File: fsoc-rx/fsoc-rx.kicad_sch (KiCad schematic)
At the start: 0 parts

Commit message: RX ROOT: power USB
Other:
- added sheet RX_POWER_USB (rx_power_usb.kicad_sch)
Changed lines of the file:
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@@
 	(generator_version "10.0")
 	(paper "A4")
+	(sheet
+		(at 44.45 35.56)
+		(size 54.61 88.9)
+		(exclude_from_sim no)
+		(in_bom yes)
+		(on_board yes)
+		(dnp no)
+		(fields_autoplaced yes)
+		(stroke
+			(width 0.1524)
+			(type solid)
+		)
+		(fill
+			(color 0 0 0 0)
+		)
+		(property "Sheetname" "RX_POWER_USB"
+			(at 44.45 34.8484 0)
+			(show_name no)
+			(do_not_autoplace no)
+			(effects
+				(font
+					(size 1.27 1.27)
+				)
+				(justify left bottom)
+			)
+		)
+		(property "Sheetfile" "rx_power_usb.kicad_sch"
+			(at 44.45 125.0446 0)
+			(show_name no)
+			(do_not_autoplace no)
+			(effects
+				(font
+					(size 1.27 1.27)
+				)
+				(justify left top)
+			)
+		)
+		(instances
+			(project "fsoc-rx"
+				(path "/84f983f4-ce6f-4382-bffe-129758307136"
+					(page "2")
+				)
+			)
+		)
+	)
 	(sheet_instances
 		(path "/"

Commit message: RX ROOT: MCU clock
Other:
- added sheet RX_MCU_CLOCK (rx_mcu_clock.kicad_sch)
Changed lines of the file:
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@@
+		)
+	)
+	(sheet
+		(at 139.7 46.99)
+		(size 63.5 74.93)
+		(exclude_from_sim no)
+		(in_bom yes)
+		(on_board yes)
+		(dnp no)
+		(fields_autoplaced yes)
+		(stroke
+			(width 0.1524)
+			(type solid)
+		)
+		(fill
+			(color 0 0 0 0)
+		)
+		(property "Sheetname" "RX_MCU_CLOCK"
+			(at 139.7 46.2784 0)
+			(show_name no)
+			(do_not_autoplace no)
+			(effects
+				(font
+					(size 1.27 1.27)
+				)
+				(justify left bottom)
+			)
+		)
+		(property "Sheetfile" "rx_mcu_clock.kicad_sch"
+			(at 139.7 122.5046 0)
+			(show_name no)
+			(do_not_autoplace no)
+			(effects
+				(font
+					(size 1.27 1.27)
+				)
+				(justify left top)
+			)
+		)
+		(instances
+			(project "fsoc-rx"
+				(path "/84f983f4-ce6f-4382-bffe-129758307136"
+					(page "3")
+				)
+			)
 		)
 	)

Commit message: RX ROOT: HOST IO
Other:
- added sheet RX_HOST_IO (rx_host_io.kicad_sch)
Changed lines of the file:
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@@
 	(paper "A4")
 	(sheet
+		(at 60.96 90.17)
+		(size 49.53 21.59)
+		(exclude_from_sim no)
+		(in_bom yes)
+		(on_board yes)
+		(dnp no)
+		(fields_autoplaced yes)
+		(stroke
+			(width 0.1524)
+			(type solid)
+		)
+		(fill
+			(color 0 0 0 0)
+		)
+		(property "Sheetname" "RX_HOST_IO"
+			(at 60.96 89.4584 0)
+			(show_name no)
+			(do_not_autoplace no)
+			(effects
+				(font
+					(size 1.27 1.27)
+				)
+				(justify left bottom)
+			)
+		)
+		(property "Sheetfile" "rx_host_io.kicad_sch"
+			(at 60.96 112.3446 0)
+			(show_name no)
+			(do_not_autoplace no)
+			(effects
+				(font
+					(size 1.27 1.27)
+				)
+				(justify left top)
+			)
+		)
+		(instances
+			(project "fsoc-rx"
+				(path "/84f983f4-ce6f-4382-bffe-129758307136"
+					(page "4")
+				)
+			)
+		)
+	)
+	(sheet
 		(at 44.45 35.56)
-		(size 54.61 88.9)
+		(size 57.15 27.94)
 		(exclude_from_sim no)
 		(in_bom yes)
@@
 		)
 		(property "Sheetfile" "rx_power_usb.kicad_sch"
-			(at 44.45 125.0446 0)
+			(at 44.45 64.0846 0)
 			(show_name no)
 			(do_not_autoplace no)
@@
 	)
 	(sheet
-		(at 139.7 46.99)
-		(size 63.5 74.93)
+		(at 124.46 36.83)
+		(size 57.15 30.48)
 		(exclude_from_sim no)
 		(in_bom yes)
@@
 		)
 		(property "Sheetname" "RX_MCU_CLOCK"
-			(at 139.7 46.2784 0)
+			(at 124.46 36.1184 0)
 			(show_name no)
 			(do_not_autoplace no)
@@
 		)
 		(property "Sheetfile" "rx_mcu_clock.kicad_sch"
-			(at 139.7 122.5046 0)
+			(at 124.46 67.8946 0)
 			(show_name no)
 			(do_not_autoplace no)

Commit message: RX ROOT: monitor
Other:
- added sheet RX_MONITOR (rx_monitor.kicad_sch)
- added sheet RX_OPTICAL_AFE (rx_optical_afe.kicad_sch)
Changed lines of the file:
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@@
 	(paper "A4")
 	(sheet
-		(at 60.96 90.17)
+		(at 44.45 83.82)
 		(size 49.53 21.59)
 		(exclude_from_sim no)
@@
 		)
 		(property "Sheetname" "RX_HOST_IO"
-			(at 60.96 89.4584 0)
+			(at 44.45 83.1084 0)
 			(show_name no)
 			(do_not_autoplace no)
@@
 		)
 		(property "Sheetfile" "rx_host_io.kicad_sch"
-			(at 60.96 112.3446 0)
+			(at 44.45 105.9946 0)
 			(show_name no)
 			(do_not_autoplace no)
@@
 				(path "/84f983f4-ce6f-4382-bffe-129758307136"
 					(page "4")
+				)
+			)
+		)
+	)
+	(sheet
+		(at 118.11 85.09)
+		(size 59.69 20.32)
+		(exclude_from_sim no)
+		(in_bom yes)
+		(on_board yes)
+		(dnp no)
+		(fields_autoplaced yes)
+		(stroke
+			(width 0.1524)
+			(type solid)
+		)
+		(fill
+			(color 0 0 0 0)
+		)
+		(property "Sheetname" "RX_OPTICAL_AFE"
+			(at 118.11 84.3784 0)
+			(show_name no)
+			(do_not_autoplace no)
+			(effects
+				(font
+					(size 1.27 1.27)
+				)
+				(justify left bottom)
+			)
+		)
+		(property "Sheetfile" "rx_optical_afe.kicad_sch"
+			(at 118.11 105.9946 0)
+			(show_name no)
+			(do_not_autoplace no)
+			(effects
+				(font
+					(size 1.27 1.27)
+				)
+				(justify left top)
+			)
+		)
+		(instances
+			(project "fsoc-rx"
+				(path "/84f983f4-ce6f-4382-bffe-129758307136"
+					(page "5")
 				)
 			)
@@
 				)
 			)
+		)
+	)
+	(sheet
+		(at 45.72 125.73)
+		(size 50.8 20.32)
+		(exclude_from_sim no)
+		(in_bom yes)
+		(on_board yes)
+		(dnp no)
+		(fields_autoplaced yes)
+		(stroke
+			(width 0.1524)
+			(type solid)
+		)
+		(fill
+			(color 0 0 0 0)
+		)
+		(property "Sheetname" "RX_MONITOR"
+			(at 45.72 125.0184 0)
+			(show_name no)
+			(do_not_autoplace no)
+			(effects
+				(font
+					(size 1.27 1.27)
+				)
+				(justify left bottom)
+			)
+		)
+		(property "Sheetfile" "rx_monitor.kicad_sch"
+			(at 45.72 146.6346 0)
+			(show_name no)
+			(do_not_autoplace no)
+			(effects
+				(font
+					(size 1.27 1.27)
+				)
+				(justify left top)
+			)
+		)
+		(instances
+			(project "fsoc-rx"
+				(path "/84f983f4-ce6f-4382-bffe-129758307136"
+					(page "6")
+				)
+			)

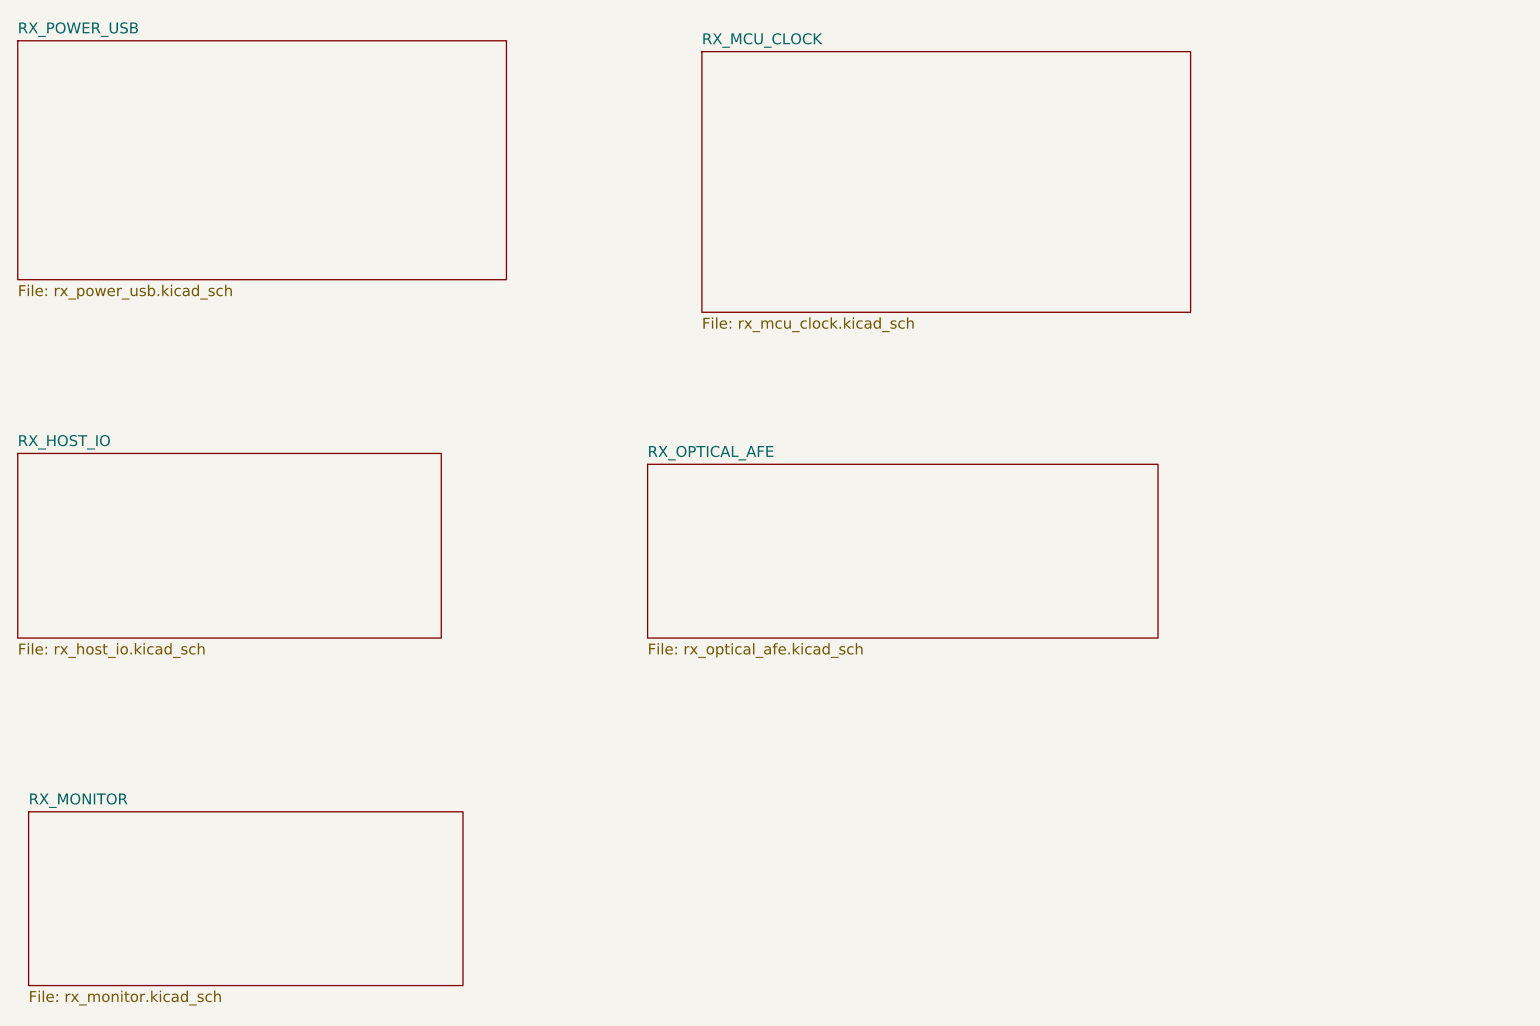
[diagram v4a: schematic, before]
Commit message: RX ROOT: optical AFE
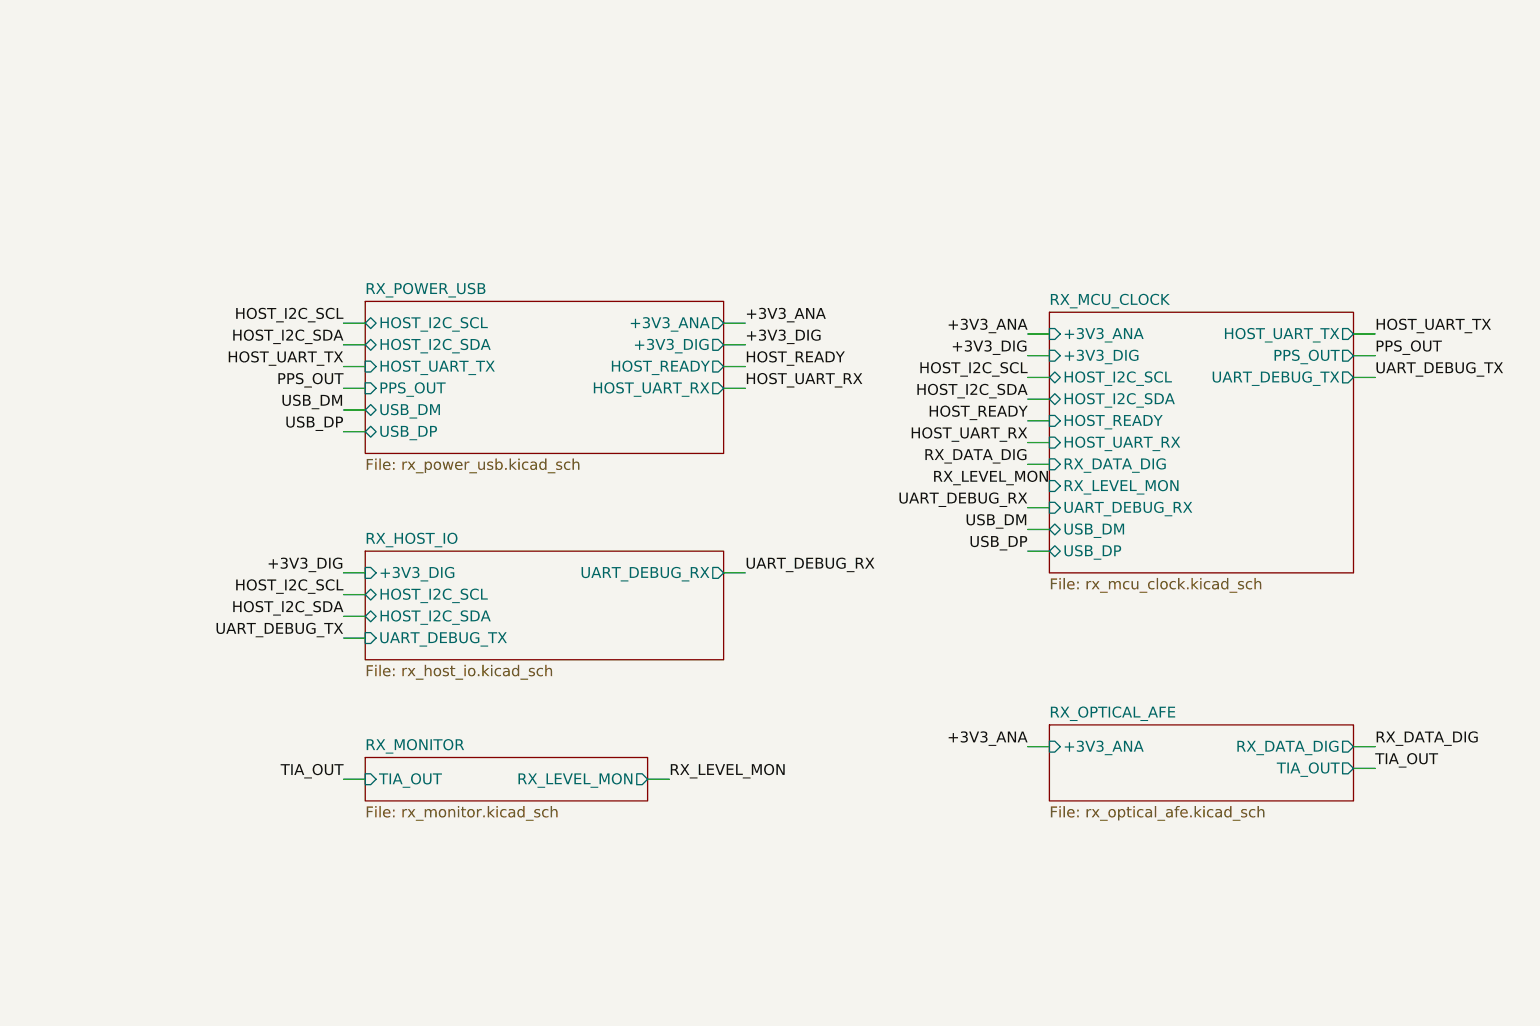
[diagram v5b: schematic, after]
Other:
- sheet RX_HOST_IO ports: added +3V3_DIG, HOST_I2C_SCL, HOST_I2C_SDA, UART_DEBUG_RX, UART_DEBUG_TX; removed none
- sheet RX_MCU_CLOCK ports: added +3V3_ANA, +3V3_DIG, HOST_I2C_SCL, HOST_I2C_SDA, HOST_READY, HOST_UART_RX, HOST_UART_TX, PPS_OUT, RX_DATA_DIG, RX_LEVEL_MON, UART_DEBUG_RX, UART_DEBUG_TX, USB_DM, USB_DP; removed none
- sheet RX_MONITOR ports: added RX_LEVEL_MON, TIA_OUT; removed none
- sheet RX_OPTICAL_AFE ports: added +3V3_ANA, RX_DATA_DIG, TIA_OUT; removed none
- sheet RX_POWER_USB ports: added +3V3_ANA, +3V3_DIG, HOST_I2C_SCL, HOST_I2C_SDA, HOST_READY, HOST_UART_RX, HOST_UART_TX, PPS_OUT, USB_DM, USB_DP; removed none

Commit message: RX PCB
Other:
- sheet RX_MCU_CLOCK ports: added USB_DN; removed USB_DM
- sheet RX_POWER_USB ports: added USB_DN; removed USB_DM
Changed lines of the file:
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@@
 		)
 	)
-	(label "USB_DM"
+	(label "USB_DN"
 		(at 162.56 92.71 180)
 		(effects
@@
 		)
 	)
-	(label "USB_DM"
+	(label "USB_DN"
 		(at 82.55 78.74 180)
 		(effects
@@
 	(sheet
 		(at 85.09 66.04)
-		(size 41.91 17.78)
+		(size 41.91 16.51)
 		(exclude_from_sim no)
 		(in_bom yes)
@@
 		)
 		(property "Sheetfile" "rx_power_usb.kicad_sch"
-			(at 85.09 84.4046 0)
+			(at 85.09 83.1346 0)
 			(show_name no)
 			(do_not_autoplace no)
@@
 			)
 		)
-		(pin "USB_DM" bidirectional
-			(at 85.09 78.74 180)
-			(effects
-				(font
-					(size 1.27 1.27)
-				)
-				(justify left)
-			)
-		)
 		(pin "USB_DP" bidirectional
 			(at 85.09 81.28 180)
@@
 				)
 				(justify right)
+			)
+		)
+		(pin "USB_DN" bidirectional
+			(at 85.09 78.74 180)
+			(effects
+				(font
+					(size 1.27 1.27)
+				)
+				(justify left)
 			)
 		)
@@
 			)
 		)
-		(pin "USB_DM" bidirectional
-			(at 165.1 92.71 180)
-			(effects
-				(font
-					(size 1.27 1.27)
-				)
-				(justify left)
-			)
-		)
 		(pin "USB_DP" bidirectional
 			(at 165.1 95.25 180)
@@
 			)
 		)
+		(pin "USB_DN" bidirectional
+			(at 165.1 92.71 180)
+			(effects
+				(font
+					(size 1.27 1.27)
+				)
+				(justify left)
+			)
+		)

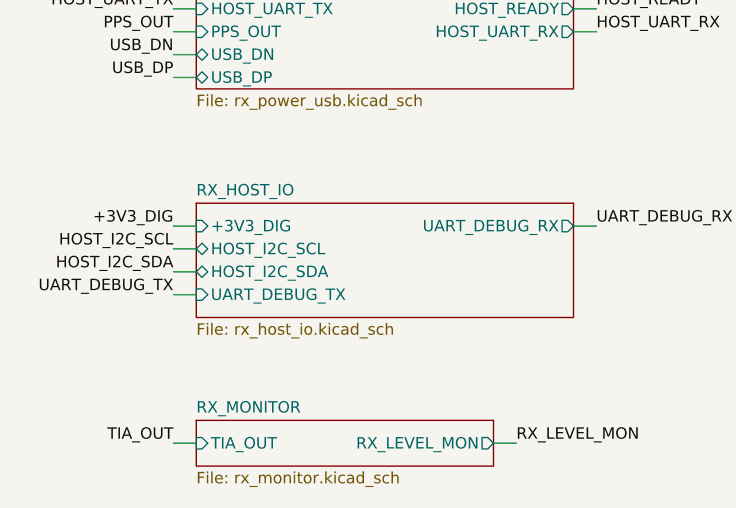
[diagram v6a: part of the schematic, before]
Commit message: RX PCB: SiT5346
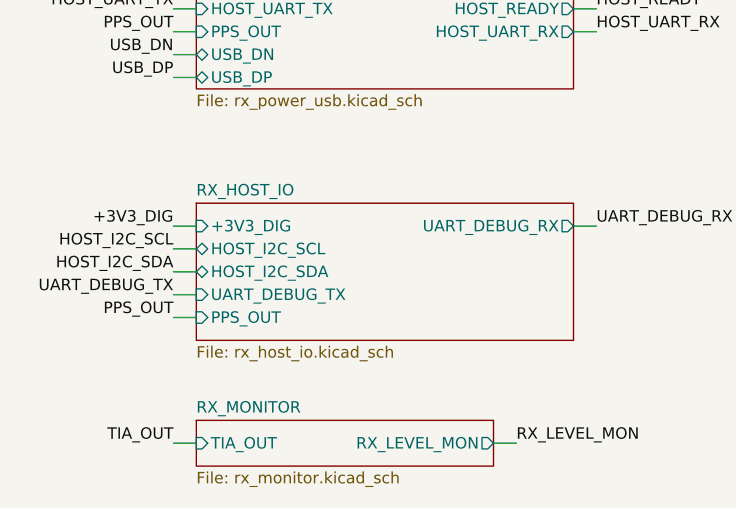
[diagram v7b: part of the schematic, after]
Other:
- sheet RX_HOST_IO ports: added PPS_OUT; removed none
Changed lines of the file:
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@@
+	(wire
+		(pts
+			(xy 82.55 107.95) (xy 85.09 107.95)
+		)
+		(stroke
+			(width 0)
+			(type default)
+		)
+	)
 	(wire
 		(pts
@@
 		)
 	)
+	(label "PPS_OUT"
+		(at 82.55 107.95 180)
+		(effects
+			(font
+				(size 1.27 1.27)
+			)
+			(justify right bottom)
+		)
+	)
 	(label "UART_DEBUG_TX"
 		(at 82.55 105.41 180)
@@
 	(sheet
 		(at 85.09 95.25)
-		(size 41.91 12.7)
+		(size 41.91 15.24)
 		(exclude_from_sim no)
 		(in_bom yes)
@@
 		)
 		(property "Sheetfile" "rx_host_io.kicad_sch"
-			(at 85.09 108.5346 0)
+			(at 85.09 111.0746 0)
 			(show_name no)
 			(do_not_autoplace no)
@@
 			)
 		)
+		(pin "PPS_OUT" input
+			(at 85.09 107.95 180)
+			(effects
+				(font
+					(size 1.27 1.27)
+				)
+				(justify left)
+			)
+		)
